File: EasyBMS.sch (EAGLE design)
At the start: 148 parts, among them Q10 BSS84LT1G, Q11 BSS84LT1G, Q12 BSS84LT1G, Q13 BSS84LT1G, Q2 BSS84LT1G, Q3 BSS84LT1G, Q4 BSS84LT1G, Q5 BSS84LT1G, Q6 BSS84LT1G, Q7 BSS84LT1G, Q8 BSS84LT1G, Q9 BSS84LT1G

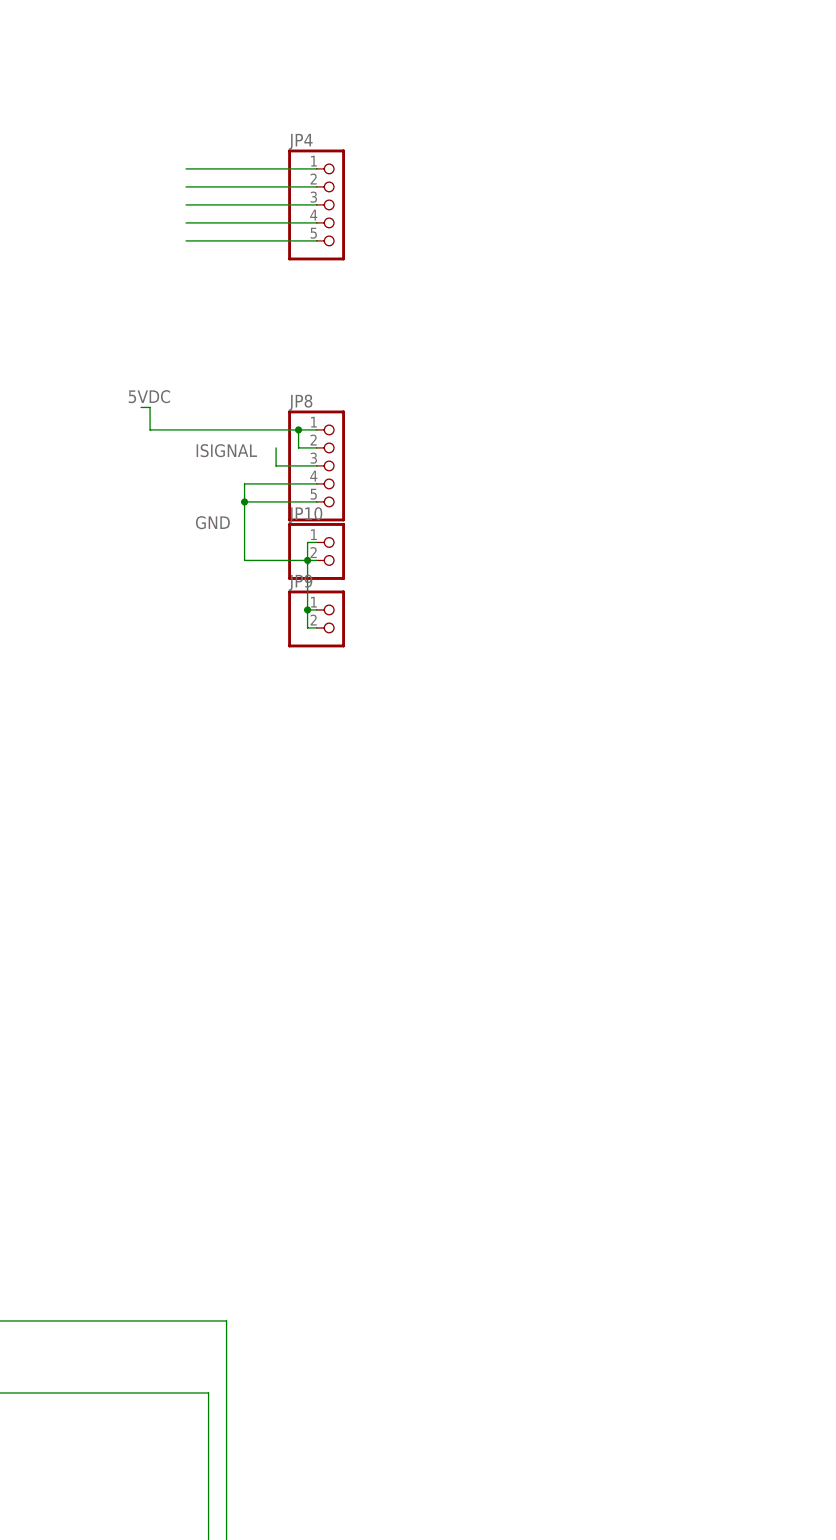
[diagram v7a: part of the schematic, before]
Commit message: new footprint for current sensor added
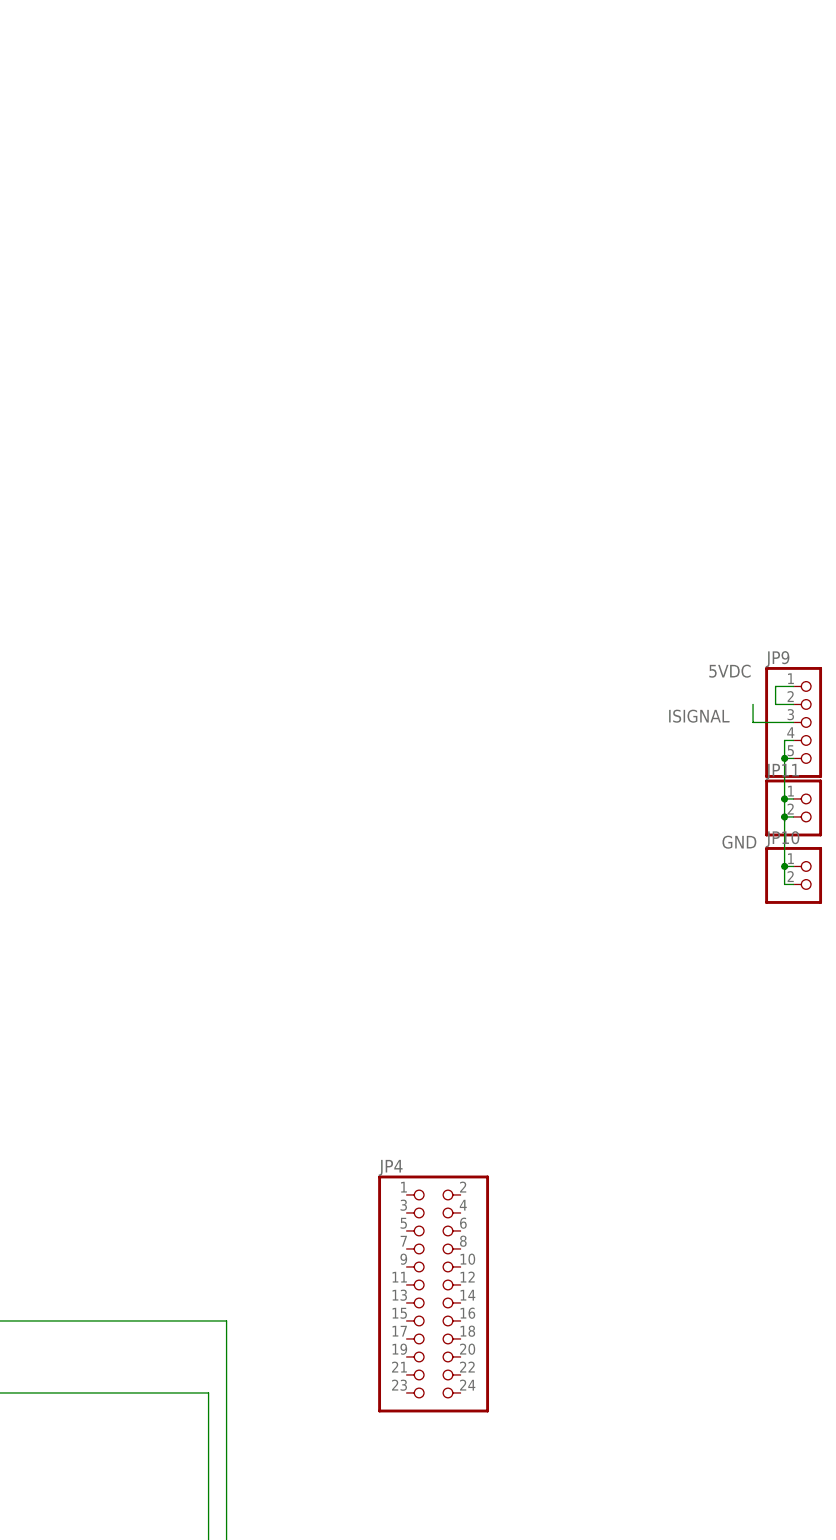
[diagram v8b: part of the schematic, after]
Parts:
- removed JP8: (no value), pinhead:PINHD-1X5
- added JP11: (no value), pinhead:PINHD-1X2
- JP4: device pinhead:PINHD-1X5 -> pinhead:PINHD-2X12
- JP9: device pinhead:PINHD-1X2 -> pinhead:PINHD-1X5
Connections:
- removed net N$15: JP4.2
- removed net N$17: JP4.3
- removed net N$18: JP4.4
- removed net N$25: JP4.5
- removed net N$7: JP4.1
- net 5VDC: now also JP9.1, JP9.2; no longer JP8.1, JP8.2
- net GND: now also JP11.1, JP11.2, JP9.4, JP9.5; no longer JP8.4, JP8.5, JP9.1, JP9.2
- net ISIGNAL: now also JP9.3; no longer JP8.3
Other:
- moved on the sheet: JP10
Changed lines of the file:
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@@
 <part name="C18" library="rcl" library_urn="urn:adsk.eagle:library:334" deviceset="C-EU" device="C1206" package3d_urn="urn:adsk.eagle:package:23618/2"/>
 <part name="C19" library="rcl" library_urn="urn:adsk.eagle:library:334" deviceset="C-EU" device="C1206" package3d_urn="urn:adsk.eagle:package:23618/2"/>
-<part name="JP8" library="pinhead" library_urn="urn:adsk.eagle:library:325" deviceset="PINHD-1X5" device="" package3d_urn="urn:adsk.eagle:package:22469/2"/>
-<part name="JP9" library="pinhead" library_urn="urn:adsk.eagle:library:325" deviceset="PINHD-1X2" device="" package3d_urn="urn:adsk.eagle:package:22435/2"/>
+<part name="JP9" library="pinhead" library_urn="urn:adsk.eagle:library:325" deviceset="PINHD-1X5" device="" package3d_urn="urn:adsk.eagle:package:22469/2"/>
 <part name="JP10" library="pinhead" library_urn="urn:adsk.eagle:library:325" deviceset="PINHD-1X2" device="" package3d_urn="urn:adsk.eagle:package:22435/2"/>
-<part name="JP4" library="pinhead" library_urn="urn:adsk.eagle:library:325" deviceset="PINHD-1X5" device="" package3d_urn="urn:adsk.eagle:package:22469/2"/>
+<part name="JP11" library="pinhead" library_urn="urn:adsk.eagle:library:325" deviceset="PINHD-1X2" device="" package3d_urn="urn:adsk.eagle:package:22435/2"/>
+<part name="JP4" library="pinhead" library_urn="urn:adsk.eagle:library:325" deviceset="PINHD-2X12" device="" package3d_urn="urn:adsk.eagle:package:22420/2"/>
 </parts>
 <sheets>
@@
 <attribute name="VALUE" x="207.264" y="25.781" size="1.778" layer="96"/>
 </instance>
-<instance part="JP8" gate="A" x="528.32" y="265.43" smashed="yes">
-<attribute name="NAME" x="521.97" y="273.685" size="1.778" layer="95"/>
-<attribute name="VALUE" x="521.97" y="257.81" size="1.778" layer="96"/>
-</instance>
-<instance part="JP9" gate="G$1" x="528.32" y="242.57" smashed="yes">
-<attribute name="NAME" x="521.97" y="248.285" size="1.778" layer="95"/>
-<attribute name="VALUE" x="521.97" y="237.49" size="1.778" layer="96"/>
-</instance>
-<instance part="JP10" gate="G$1" x="528.32" y="252.095" smashed="yes">
-<attribute name="NAME" x="521.97" y="257.81" size="1.778" layer="95"/>
-<attribute name="VALUE" x="521.97" y="247.015" size="1.778" layer="96"/>
-</instance>
-<instance part="JP4" gate="A" x="528.32" y="302.26" smashed="yes">
-<attribute name="NAME" x="521.97" y="310.515" size="1.778" layer="95"/>
-<attribute name="VALUE" x="521.97" y="294.64" size="1.778" layer="96"/>
+<instance part="JP9" gate="A" x="595.63" y="229.235" smashed="yes">
+<attribute name="NAME" x="589.28" y="237.49" size="1.778" layer="95"/>
+<attribute name="VALUE" x="589.28" y="221.615" size="1.778" layer="96"/>
+</instance>
+<instance part="JP10" gate="G$1" x="595.63" y="206.375" smashed="yes">
+<attribute name="NAME" x="589.28" y="212.09" size="1.778" layer="95"/>
+<attribute name="VALUE" x="589.28" y="201.295" size="1.778" layer="96"/>
+</instance>
+<instance part="JP11" gate="G$1" x="595.63" y="215.9" smashed="yes">
+<attribute name="NAME" x="589.28" y="221.615" size="1.778" layer="95"/>
+<attribute name="VALUE" x="589.28" y="210.82" size="1.778" layer="96"/>
+</instance>
+<instance part="JP4" gate="A" x="541.02" y="149.86" smashed="yes">
+<attribute name="NAME" x="534.67" y="165.735" size="1.778" layer="95"/>
+<attribute name="VALUE" x="534.67" y="129.54" size="1.778" layer="96"/>
 </instance>
 </instances>
@@
 </segment>
 <segment>
-<pinref part="JP8" gate="A" pin="1"/>
-<wire x1="525.78" y1="270.51" x2="523.24" y2="270.51" width="0.1524" layer="91"/>
-<pinref part="JP8" gate="A" pin="2"/>
-<wire x1="525.78" y1="267.97" x2="523.24" y2="267.97" width="0.1524" layer="91"/>
-<wire x1="523.24" y1="267.97" x2="523.24" y2="270.51" width="0.1524" layer="91"/>
-<wire x1="523.24" y1="270.51" x2="502.285" y2="270.51" width="0.1524" layer="91"/>
-<junction x="523.24" y="270.51"/>
-<wire x1="502.285" y1="270.51" x2="502.285" y2="273.685" width="0.1524" layer="91"/>
-<wire x1="502.285" y1="273.685" x2="501.015" y2="273.685" width="0.1524" layer="91"/>
-<label x="499.11" y="274.32" size="1.778" layer="95"/>
+<pinref part="JP9" gate="A" pin="1"/>
+<wire x1="593.09" y1="234.315" x2="590.55" y2="234.315" width="0.1524" layer="91"/>
+<pinref part="JP9" gate="A" pin="2"/>
+<wire x1="593.09" y1="231.775" x2="590.55" y2="231.775" width="0.1524" layer="91"/>
+<wire x1="590.55" y1="231.775" x2="590.55" y2="234.315" width="0.1524" layer="91"/>
+<label x="581.025" y="235.585" size="1.778" layer="95"/>
 </segment>
 </net>
@@
 </segment>
 <segment>
-<pinref part="JP9" gate="G$1" pin="2"/>
-<wire x1="524.51" y1="242.57" x2="525.78" y2="242.57" width="0.1524" layer="91"/>
-<pinref part="JP9" gate="G$1" pin="1"/>
-<wire x1="524.51" y1="245.11" x2="525.78" y2="245.11" width="0.1524" layer="91"/>
-<junction x="524.51" y="245.11"/>
-<wire x1="524.51" y1="245.11" x2="524.51" y2="242.57" width="0.1524" layer="91"/>
 <pinref part="JP10" gate="G$1" pin="2"/>
+<wire x1="591.82" y1="206.375" x2="593.09" y2="206.375" width="0.1524" layer="91"/>
 <pinref part="JP10" gate="G$1" pin="1"/>
-<wire x1="524.51" y1="254.635" x2="525.78" y2="254.635" width="0.1524" layer="91"/>
-<wire x1="524.51" y1="254.635" x2="524.51" y2="252.095" width="0.1524" layer="91"/>
-<wire x1="524.51" y1="252.095" x2="525.78" y2="252.095" width="0.1524" layer="91"/>
-<junction x="524.51" y="252.095"/>
-<wire x1="524.51" y1="252.095" x2="524.51" y2="245.11" width="0.1524" layer="91"/>
-<wire x1="524.51" y1="252.095" x2="524.51" y2="251.46" width="0.1524" layer="91"/>
-<pinref part="JP8" gate="A" pin="5"/>
-<pinref part="JP8" gate="A" pin="4"/>
-<wire x1="525.78" y1="262.89" x2="515.62" y2="262.89" width="0.1524" layer="91"/>
-<wire x1="515.62" y1="262.89" x2="515.62" y2="260.35" width="0.1524" layer="91"/>
-<wire x1="515.62" y1="260.35" x2="525.78" y2="260.35" width="0.1524" layer="91"/>
-<wire x1="524.51" y1="252.095" x2="515.62" y2="252.095" width="0.1524" layer="91"/>
-<wire x1="515.62" y1="252.095" x2="515.62" y2="260.35" width="0.1524" layer="91"/>
-<junction x="515.62" y="260.35"/>
-<label x="508.635" y="256.54" size="1.778" layer="95"/>
+<wire x1="591.82" y1="208.915" x2="593.09" y2="208.915" width="0.1524" layer="91"/>
+<junction x="591.82" y="208.915"/>
+<wire x1="591.82" y1="208.915" x2="591.82" y2="206.375" width="0.1524" layer="91"/>
+<pinref part="JP11" gate="G$1" pin="2"/>
+<pinref part="JP11" gate="G$1" pin="1"/>
+<wire x1="591.82" y1="218.44" x2="593.09" y2="218.44" width="0.1524" layer="91"/>
+<wire x1="591.82" y1="218.44" x2="591.82" y2="215.9" width="0.1524" layer="91"/>
+<wire x1="591.82" y1="215.9" x2="593.09" y2="215.9" width="0.1524" layer="91"/>
+<junction x="591.82" y="215.9"/>
+<wire x1="591.82" y1="215.9" x2="591.82" y2="208.915" width="0.1524" layer="91"/>
+<wire x1="591.82" y1="215.9" x2="591.82" y2="215.265" width="0.1524" layer="91"/>
+<pinref part="JP9" gate="A" pin="4"/>
+<wire x1="593.09" y1="226.695" x2="591.82" y2="226.695" width="0.1524" layer="91"/>
+<wire x1="591.82" y1="226.695" x2="591.82" y2="224.155" width="0.1524" layer="91"/>
+<junction x="591.82" y="218.44"/>
+<pinref part="JP9" gate="A" pin="5"/>
+<wire x1="591.82" y1="224.155" x2="591.82" y2="218.44" width="0.1524" layer="91"/>
+<wire x1="593.09" y1="224.155" x2="591.82" y2="224.155" width="0.1524" layer="91"/>
+<junction x="591.82" y="224.155"/>
+<label x="582.93" y="211.455" size="1.778" layer="95"/>
 </segment>
 </net>
@@
 <net name="ISIGNAL" class="0">
 <segment>
-<pinref part="JP8" gate="A" pin="3"/>
-<wire x1="525.78" y1="265.43" x2="520.065" y2="265.43" width="0.1524" layer="91"/>
-<wire x1="520.065" y1="265.43" x2="520.065" y2="267.97" width="0.1524" layer="91"/>
-<label x="508.635" y="266.7" size="1.778" layer="95"/>
-</segment>
-<segment>
 <label x="208.28" y="314.96" size="1.778" layer="95"/>
 <wire x1="210.82" y1="314.96" x2="142.24" y2="314.96" width="0.1524" layer="91"/>
 <pinref part="JP5" gate="A" pin="24"/>
 </segment>
-</net>
-<net name="N$7" class="0">
-<segment>
-<pinref part="JP4" gate="A" pin="1"/>
-<wire x1="525.78" y1="307.34" x2="507.365" y2="307.34" width="0.1524" layer="91"/>
-</segment>
-</net>
-<net name="N$15" class="0">
-<segment>
-<pinref part="JP4" gate="A" pin="2"/>
-<wire x1="525.78" y1="304.8" x2="507.365" y2="304.8" width="0.1524" layer="91"/>
-</segment>
-</net>
-<net name="N$17" class="0">
-<segment>
-<pinref part="JP4" gate="A" pin="3"/>
-<wire x1="525.78" y1="302.26" x2="507.365" y2="302.26" width="0.1524" layer="91"/>
-</segment>
-</net>
-<net name="N$18" class="0">
-<segment>
-<pinref part="JP4" gate="A" pin="4"/>
-<wire x1="525.78" y1="299.72" x2="507.365" y2="299.72" width="0.1524" layer="91"/>
-</segment>
-</net>
-<net name="N$25" class="0">
-<segment>
-<pinref part="JP4" gate="A" pin="5"/>
-<wire x1="525.78" y1="297.18" x2="507.365" y2="297.18" width="0.1524" layer="91"/>
-</segment>
-</net>
+<segment>
+<pinref part="JP9" gate="A" pin="3"/>
+<wire x1="593.09" y1="229.235" x2="587.375" y2="229.235" width="0.1524" layer="91"/>
+<wire x1="587.375" y1="229.235" x2="587.375" y2="231.775" width="0.1524" layer="91"/>
+<label x="575.31" y="229.235" size="1.778" layer="95"/>
+</segment>
+</net>
